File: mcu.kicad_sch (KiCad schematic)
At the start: 6 parts, among them U1 WIFI_KIT_32__V3_

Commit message: Push schematic stuff missed before.
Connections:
- net +3.3V is gone; now on net +3V3: D3.1 (A1)
- net +3V3: no longer U1.J3_2 (3V3), U1.J3_3 (3V3)
- new net +3V3MCU: U1.J3_2 (3V3), U1.J3_3 (3V3)
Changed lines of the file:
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@@
+		)
+	)
+	(hierarchical_label "+3V3MCU"
+		(shape input)
+		(at 173.99 55.88 90)
+		(effects
+			(font
+				(size 1.27 1.27)
+			)
+			(justify left)
 		)
 	)
@@
 	)
 	(symbol
-		(lib_id "power:+3V3")
-		(at 173.99 55.88 0)
-		(unit 1)
-		(exclude_from_sim no)
-		(in_bom yes)
-		(on_board yes)
-		(dnp no)
-		(fields_autoplaced yes)
-		(property "Reference" "#PWR01"
-			(at 173.99 59.69 0)
-			(effects
-				(font
-					(size 1.27 1.27)
-				)
-				(hide yes)
-			)
-		)
-		(property "Value" "+3V3"
-			(at 173.99 50.8 0)
-			(effects
-				(font
-					(size 1.27 1.27)
-				)
-			)
-		)
-		(property "Footprint" ""
-			(at 173.99 55.88 0)
-			(effects
-				(font
-					(size 1.27 1.27)
-				)
-				(hide yes)
-			)
-		)
-		(property "Datasheet" ""
-			(at 173.99 55.88 0)
-			(effects
-				(font
-					(size 1.27 1.27)
-				)
-				(hide yes)
-			)
-		)
-		(property "Description" "Power symbol creates a global label with name \"+3V3\""
-			(at 173.99 55.88 0)
-			(effects
-				(font
-					(size 1.27 1.27)
-				)
-				(hide yes)
-			)
-		)
-		(pin "1"
-		)
-		(instances
-			(project ""
-				(path "/4ab90003-ea4c-4878-8117-f834ac24f8d9/8dddb553-bb71-4d14-8f8b-c1b446e0dbb3"
-					(reference "#PWR01")
-					(unit 1)
-				)
-			)
-		)
-	)
-	(symbol
-		(lib_id "power:+3.3V")
-		(at 116.84 25.4 270)
-		(unit 1)
-		(exclude_from_sim no)
-		(in_bom yes)
-		(on_board yes)
-		(dnp no)
-		(property "Reference" "#PWR041"
-			(at 113.03 25.4 0)
-			(effects
-				(font
-					(size 1.27 1.27)
-				)
-				(hide yes)
-			)
-		)
-		(property "Value" "+3.3V"
-			(at 122.682 25.146 90)
-			(effects
-				(font
-					(size 1.27 1.27)
-				)
-			)
-		)
-		(property "Footprint" ""
-			(at 116.84 25.4 0)
-			(effects
-				(font
-					(size 1.27 1.27)
-				)
-				(hide yes)
-			)
-		)
-		(property "Datasheet" ""
-			(at 116.84 25.4 0)
-			(effects
-				(font
-					(size 1.27 1.27)
-				)
-				(hide yes)
-			)
-		)
-		(property "Description" "Power symbol creates a global label with name \"+3.3V\""
-			(at 116.84 25.4 0)
-			(effects
-				(font
-					(size 1.27 1.27)
-				)
-				(hide yes)
-			)
-		)
-		(pin "1"
-		)
-		(instances
-			(project "stopnu-hardware"
-				(path "/4ab90003-ea4c-4878-8117-f834ac24f8d9/8dddb553-bb71-4d14-8f8b-c1b446e0dbb3"
-					(reference "#PWR041")
-					(unit 1)
-				)
-			)
-		)
-	)
-	(symbol
 		(lib_id "power:+5V")
 		(at 49.53 57.15 0)
@@
 					(unit 1)
 				)
+			)
+		)
+	)
+	(symbol
+		(lib_id "power:+3V3")
+		(at 116.84 25.4 270)
+		(unit 1)
+		(exclude_from_sim no)
+		(in_bom yes)
+		(on_board yes)
+		(dnp no)
+		(fields_autoplaced yes)
+		(property "Reference" "#PWR033"
+			(at 113.03 25.4 0)
+			(effects
+				(font
+					(size 1.27 1.27)
+				)
+				(hide yes)
+			)
+		)
+		(property "Value" "+3V3"
+			(at 120.65 25.3999 90)
+			(effects
+				(font
+					(size 1.27 1.27)
+				)
+				(justify left)
+			)
+		)
+		(property "Footprint" ""
+			(at 116.84 25.4 0)
+			(effects
+				(font
+					(size 1.27 1.27)
+				)
+				(hide yes)
+			)
+		)
+		(property "Datasheet" ""
+			(at 116.84 25.4 0)
+			(effects
+				(font
+					(size 1.27 1.27)
+				)
+				(hide yes)
+			)
+		)
+		(property "Description" "Power symbol creates a global label with name \"+3V3\""
+			(at 116.84 25.4 0)
+			(effects
+				(font
+					(size 1.27 1.27)
+				)
+				(hide yes)
+			)
+		)
+		(pin "1"
+		)
+		(instances
+			(project "stopnu-hardware"
+				(path "/4ab90003-ea4c-4878-8117-f834ac24f8d9/8dddb553-bb71-4d14-8f8b-c1b446e0dbb3"
+					(reference "#PWR033")
+					(unit 1)
+				)

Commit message: Some extra work for building the rats nest.
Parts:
- U1: symbol WIFI_KIT_32__V3_:WIFI_KIT_32__V3_ -> WIFI_KIT_32__V3_1:WIFI_KIT_32__V3_; now in the parts list
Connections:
- net GPIO45 is gone; now on net GPIO06: U1.J3_17 (GPIO6/ADC1_CH5/TOUCH6)
- net GPIO46 is gone; now on net GPIO07: U1.J3_18 (GPIO7/ADC1_CH6/TOUCH7)
- net GPIO04: now also U1.J3_15 (GPIO4/ADC1_CH3/TOUCH4); no longer U1.J2_15 (GPIO4/ADC1_CH3/TOUCH4)
- net GPIO05: now also U1.J3_16 (GPIO5/ADC1_CH4/TOUCH5); no longer U1.J2_14 (GPIO5/ADC1_CH4/TOUCH5)
- net GPIO06: no longer U1.J2_13 (GPIO6/ADC1_CH5/TOUCH6)
- net GPIO07: no longer U1.J2_12 (GPIO7/ADC1_CH6/TOUCH7)
- net GPIO33: now also U1.J2_12 (GPIO33/SPII04/FSPIHD/SUBSPIHD); no longer U1.J3_7 (GPIO33/SPIIO4/FSPIHD/SUBSPIHD)
- net GPIO47: now also U1.J2_13 (GPIO47); no longer U1.J3_6 (GPIO47)
- net GPIO48: now also U1.J2_14 (GPIO48); no longer U1.J3_5 (GPIO48)
- net USB_D+: now reaches U1.J2_10 (GPIO35/SPII06/FSPID/SUBSPID/LED_Write)
- net USB_D-: now reaches U1.J2_11 (GPIO34/SPII05/FSPCICS0/SUBSPICS0)
- net UART_TX: now reaches TP1.1, U1.J2_5 (U0RXD/GPIO44/CP2102_TX)
- net UART_RX: now reaches TP2.1, U1.J2_6 (U0TXD/GPIO43/CP2102_RX)
- net USER_KEY: now reaches U1.J2_8 (GPIO0/USER_SW)
- net OLED_RST: now reaches U1.J2_9 (GPIO36/SPII07/FSPICLK/SUBSPICLK/Vext_Ctrl)
- net GPIO01: now reaches U1.J3_12 (GPIO1/ADC1_CH0/VBAT_Read/TOUCH1)
- net GPIO02: now reaches U1.J3_13 (GPIO2/ADC1_CH1/TOUCH2)
- net GPIO03: now reaches U1.J3_14 (GPIO3/ADC1_CH2/TOUCH3)
- net GPIO34 renamed GPIO41
- net GPIO35 renamed GPIO40
- net GPIO36 renamed GPIO39
- net GPIO37 renamed GPIO38
- new net GPIO26: U1.J2_15 (GPIO26/SPICS1)
- new net GPIO42: U1.J3_7 (GPIO42/MTMS)
- no-connect marks 12 -> 5
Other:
- moved on the sheet: TP1, TP2

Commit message: WIP: Routed version, for first feedback round
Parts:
- TP1: value TestPoint -> MCU_TX
- TP2: value TestPoint -> MCU_RX
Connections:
- net +3V3MCU renamed +3V3_MCU
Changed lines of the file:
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@@
 		)
 	)
-	(hierarchical_label "+3V3MCU"
+	(hierarchical_label "+3V3_MCU"
 		(shape input)
 		(at 173.99 55.88 90)
@@
 			)
 		)
-		(property "Value" "TestPoint"
+		(property "Value" "MCU_RX"
 			(at 36.83 48.7679 0)
 			(effects
@@
 			)
 		)
-		(property "Value" "TestPoint"
+		(property "Value" "MCU_TX"
 			(at 40.64 43.6879 0)
 			(effects

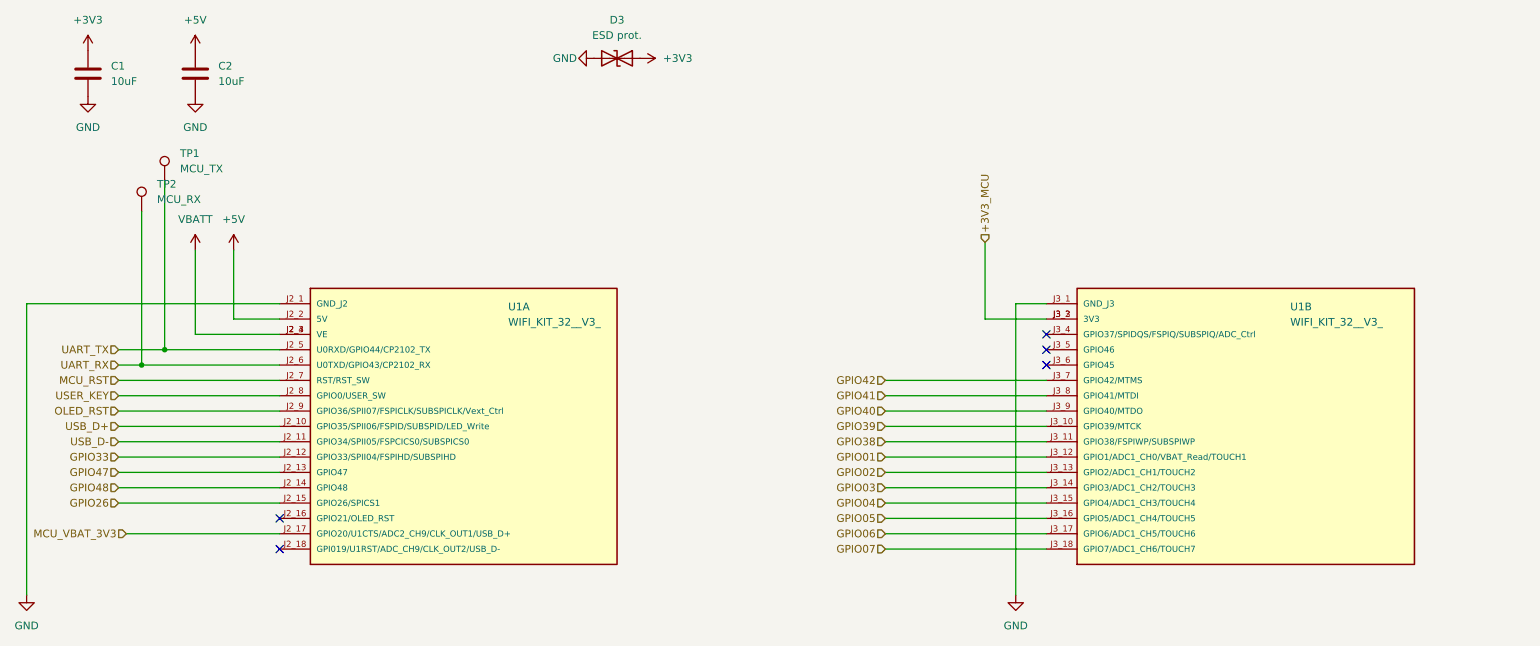
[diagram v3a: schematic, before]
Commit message: Fixed some pinout issues.
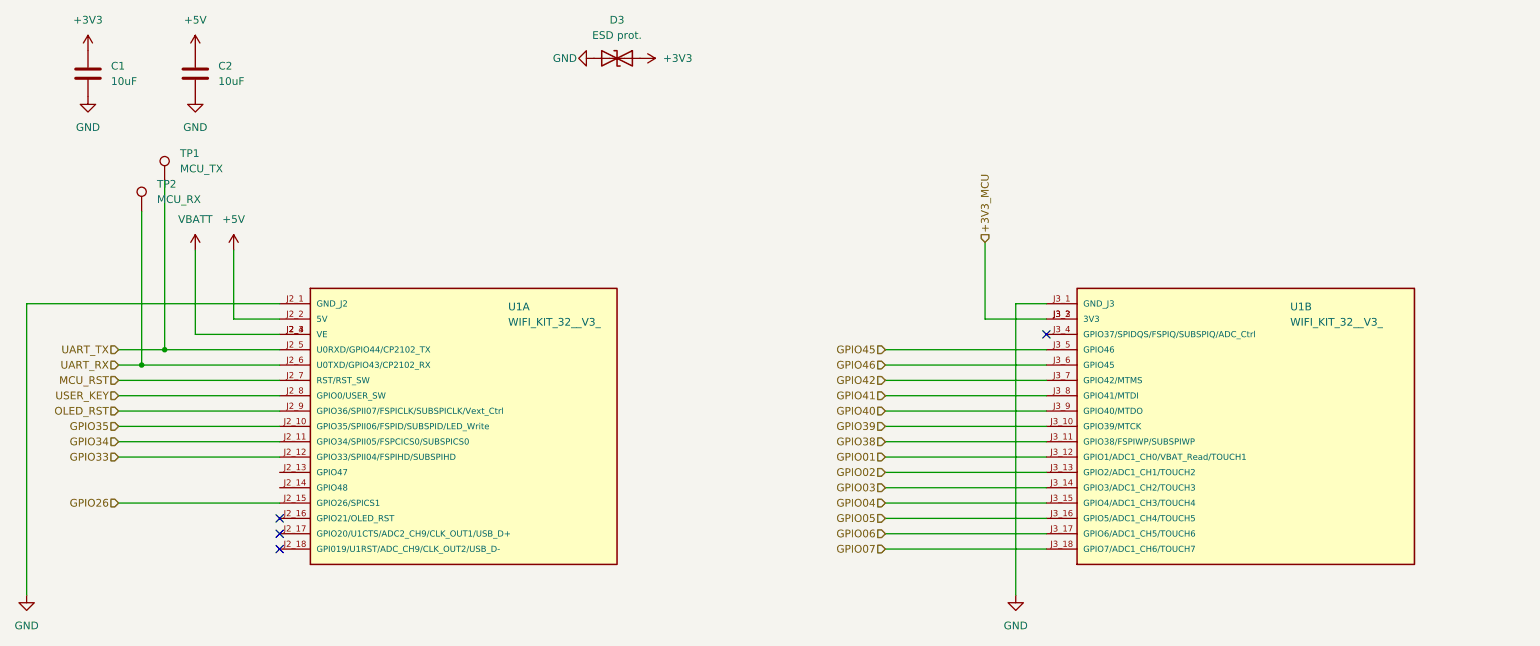
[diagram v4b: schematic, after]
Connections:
- net GPIO45: now reaches U1.J3_5 (GPIO46)
- net GPIO46: now reaches U1.J3_6 (GPIO45)
- net GPIO47: no longer names the net of U1.J2_13 (GPIO47)
- net GPIO48: no longer names the net of U1.J2_14 (GPIO48)
- net MCU_VBAT_3V3: no longer names the net of U1.J2_17 (GPIO20/U1CTS/ADC2_CH9/CLK_OUT1/USB_D+)
- net USB_D+ renamed GPIO35
- net USB_D- renamed GPIO34
- no-connect marks 5 -> 4
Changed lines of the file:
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@@
-	)
-	(no_connect
-		(at 184.15 76.2)
-	)
-	(no_connect
-		(at 184.15 73.66)
 	)
 	(no_connect
 		(at 57.15 106.68)
 	)
+	(no_connect
+		(at 57.15 104.14)
+	)
 	(wire
 		(pts
@@
 	(wire
 		(pts
-			(xy 31.75 104.14) (xy 57.15 104.14)
+			(xy 30.48 88.9) (xy 57.15 88.9)
 		)
 		(stroke
@@
 	(wire
 		(pts
-			(xy 30.48 88.9) (xy 57.15 88.9)
-		)
-		(stroke
-			(width 0)
-			(type default)
-		)
-	)
-	(wire
-		(pts
 			(xy 30.48 81.28) (xy 57.15 81.28)
 		)
@@
 	(wire
 		(pts
+			(xy 30.48 86.36) (xy 57.15 86.36)
+		)
+		(stroke
+			(width 0)
+			(type default)
+		)
+	)
+	(wire
+		(pts
 			(xy 34.29 76.2) (xy 57.15 76.2)
 		)
@@
 	(wire
 		(pts
-			(xy 30.48 96.52) (xy 57.15 96.52)
+			(xy 157.48 76.2) (xy 184.15 76.2)
 		)
 		(stroke
@@
 	(wire
 		(pts
-			(xy 30.48 86.36) (xy 57.15 86.36)
-		)
-		(stroke
-			(width 0)
-			(type default)
-		)
-	)
-	(wire
-		(pts
 			(xy 30.48 78.74) (xy 57.15 78.74)
 		)
@@
 	(wire
 		(pts
-			(xy 30.48 93.98) (xy 57.15 93.98)
-		)
-		(stroke
-			(width 0)
-			(type default)
-		)
-	)
-	(hierarchical_label "GPIO47"
-		(shape input)
-		(at 30.48 93.98 180)
+			(xy 157.48 73.66) (xy 184.15 73.66)
+		)
+		(stroke
+			(width 0)
+			(type default)
+		)
+	)
+	(hierarchical_label "GPIO45"
+		(shape input)
+		(at 157.48 73.66 180)
 		(effects
 			(font
@@
 		)
 	)
-	(hierarchical_label "MCU_VBAT_3V3"
-		(shape input)
-		(at 31.75 104.14 180)
-		(effects
-			(font
-				(size 1.27 1.27)
-			)
-			(justify right)
-		)
-	)
 	(hierarchical_label "GPIO42"
 		(shape input)
@@
 		)
 	)
-	(hierarchical_label "GPIO48"
-		(shape input)
-		(at 30.48 96.52 180)
+	(hierarchical_label "GPIO46"
+		(shape input)
+		(at 157.48 76.2 180)
 		(effects
 			(font
@@
 		)
 	)
+	(hierarchical_label "GPIO35"
+		(shape input)
+		(at 30.48 86.36 180)
+		(effects
+			(font
+				(size 1.27 1.27)
+			)
+			(justify right)
+		)
+	)
 	(hierarchical_label "GPIO04"
 		(shape input)
@@
 		)
 	)
-	(hierarchical_label "USB_D-"
+	(hierarchical_label "GPIO39"
+		(shape input)
+		(at 157.48 86.36 180)
+		(effects
+			(font
+				(size 1.27 1.27)
+			)
+			(justify right)
+		)
+	)
+	(hierarchical_label "GPIO34"
 		(shape input)
 		(at 30.48 88.9 180)
 		(effects
 			(font
-				(size 1.27 1.27)
-			)
-			(justify right)
-		)
-	)
-	(hierarchical_label "GPIO39"
-		(shape input)
-		(at 157.48 86.36 180)
-		(effects
-			(font
-				(size 1.27 1.27)
-			)
-			(justify right)
-		)
-	)
-	(hierarchical_label "USB_D+"
-		(shape input)
-		(at 30.48 86.36 180)
-		(effects
-			(font

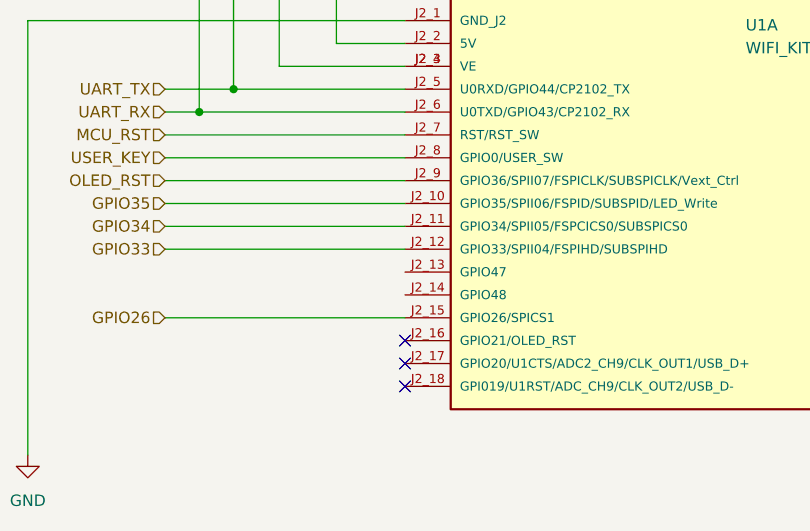
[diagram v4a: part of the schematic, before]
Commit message: Add README.md, make power input more intuitive in schematic.
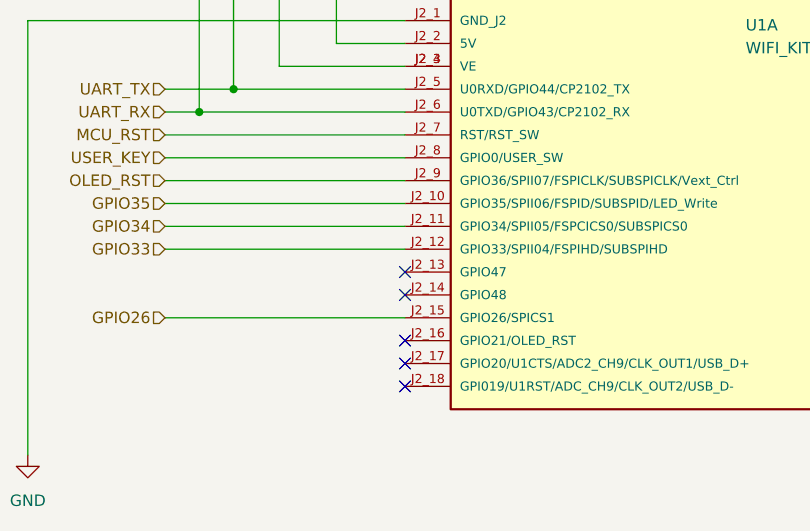
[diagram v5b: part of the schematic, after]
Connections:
- no-connect marks 4 -> 6
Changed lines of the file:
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@@
+	)
+	(no_connect
+		(at 57.15 96.52)
 	)
 	(no_connect
@@
 		(at 57.15 104.14)
 	)
+	(no_connect
+		(at 57.15 93.98)
+	)
 	(wire

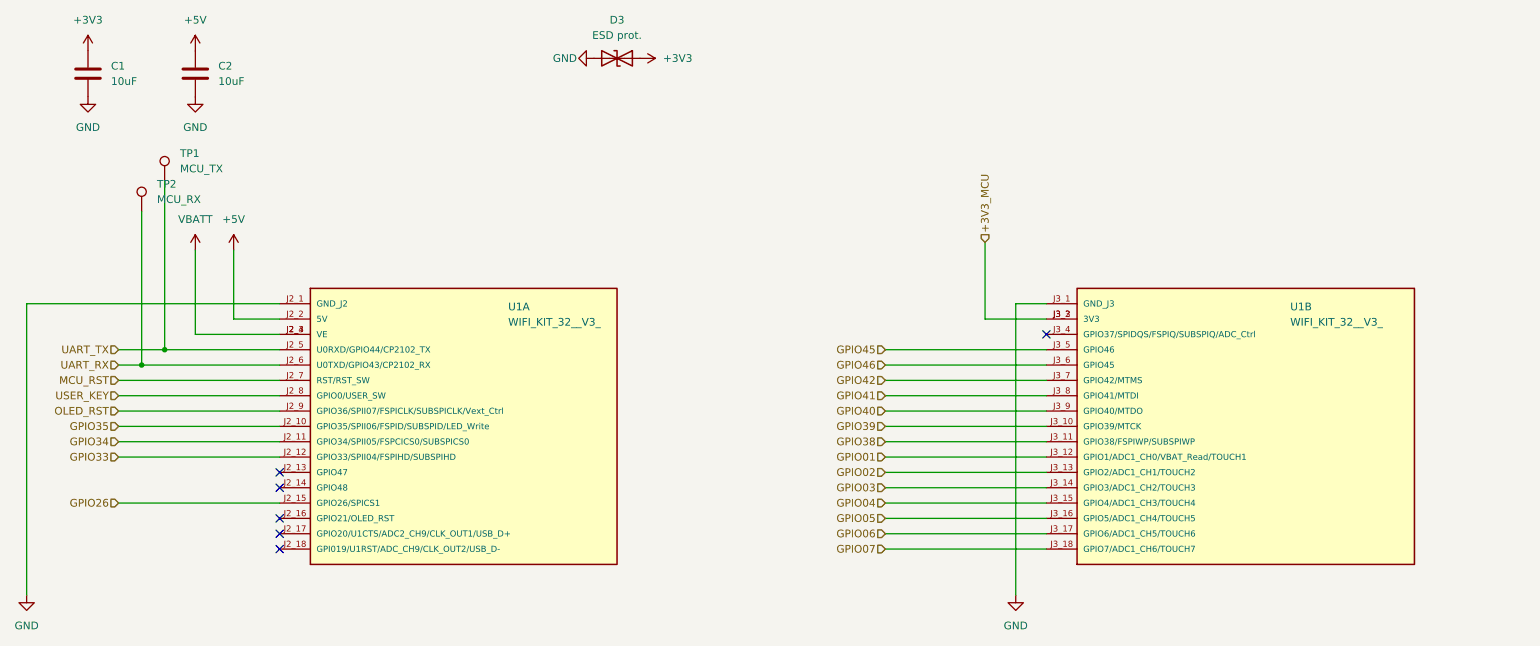
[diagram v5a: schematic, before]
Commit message: Fixed fabrication files, so PCBA will work with the correct rotation of the components.
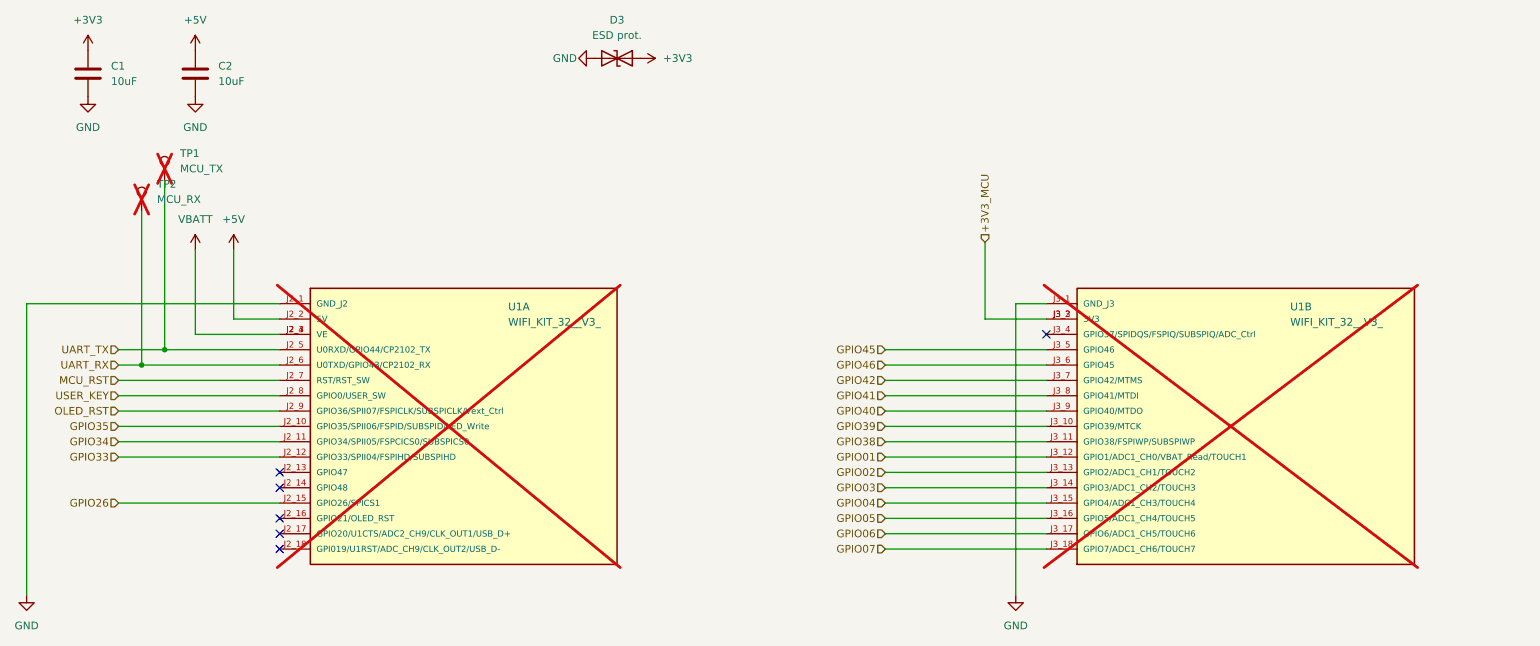
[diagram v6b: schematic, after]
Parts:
- C1, C2: LCSC C1713 -> C440198
- TP1, TP2, U1: now not fitted; now left out of the parts list
